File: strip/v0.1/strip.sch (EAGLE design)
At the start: 96 parts, among them IC1 LP2992, IC2 ADP3110A-SO8, IC3 STM32-M-48, IC4 OPA335, IC5 ADP3110A-SO8, IC6 ADP3110A-SO8, Q1 IRF7828, Q2 IRF7828, Q3 IRF7828, Q4 IRF7828, Q5 IRF7828, Q6 IRF7828

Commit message: All airwires routed. Now polishing can begin.
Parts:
- removed R32: 1k, pel_dipol_comp:RESISTOR-0402
- removed TH1: 2kOhm, pel_dipol_comp:RESISTOR-0402
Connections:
- removed net TEMP: IC3.PA5-SPI1SCK/ADC5, R32.2, TH1.1
- net +3V3: no longer R32.1
- net GND: no longer TH1.2
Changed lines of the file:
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@@
 <part name="GND16" library="supply1" deviceset="GND" device=""/>
 <part name="GND20" library="supply1" deviceset="GND" device=""/>
-<part name="TH1" library="pel_dipol_comp" deviceset="RESISTOR" device="-0402" value="2kOhm"/>
-<part name="R32" library="pel_dipol_comp" deviceset="RESISTOR" device="-0402" value="1k"/>
-<part name="P+6" library="supply1" deviceset="+3V3" device=""/>
-<part name="GND21" library="supply1" deviceset="GND" device=""/>
 <part name="L1" library="res_cap" deviceset="INDUCTOR" device="-0603" value=""/>
 <part name="C19" library="pel_dipol_comp" deviceset="CAPACITOR" device="-0402" value="100nF"/>
@@
 <instance part="GND16" gate="1" x="317.5" y="40.64"/>
 <instance part="GND20" gate="1" x="312.42" y="60.96"/>
-<instance part="TH1" gate="G$1" x="236.22" y="116.84" rot="R270"/>
-<instance part="R32" gate="G$1" x="236.22" y="127" rot="R270"/>
-<instance part="P+6" gate="G$1" x="236.22" y="137.16"/>
-<instance part="GND21" gate="1" x="236.22" y="109.22"/>
 <instance part="L1" gate="G$1" x="325.12" y="101.6" rot="R180"/>
 <instance part="C19" gate="G$1" x="335.28" y="93.98" rot="R270"/>
@@
 </segment>
 <segment>
-<pinref part="TH1" gate="G$1" pin="2"/>
-<pinref part="GND21" gate="1" pin="GND"/>
-</segment>
-<segment>
 <wire x1="60.96" y1="88.9" x2="58.42" y2="88.9" width="0.1524" layer="91"/>
 <wire x1="58.42" y1="88.9" x2="58.42" y2="83.82" width="0.1524" layer="91"/>
@@
 </segment>
 <segment>
-<wire x1="236.22" y1="134.62" x2="236.22" y2="132.08" width="0.1524" layer="91"/>
-<pinref part="R32" gate="G$1" pin="1"/>
-<pinref part="P+6" gate="G$1" pin="+3V3"/>
-</segment>
-<segment>
 <wire x1="60.96" y1="96.52" x2="58.42" y2="96.52" width="0.1524" layer="91"/>
 <wire x1="58.42" y1="96.52" x2="58.42" y2="99.06" width="0.1524" layer="91"/>
@@
 </segment>
 </net>
-<net name="TEMP" class="0">
-<segment>
-<wire x1="63.5" y1="167.64" x2="45.72" y2="167.64" width="0.1524" layer="91"/>
-<label x="63.5" y="167.64" size="1.778" layer="95" rot="MR0"/>
-<pinref part="IC3" gate="G$1" pin="PA5-SPI1SCK/ADC5"/>
-</segment>
-<segment>
-<wire x1="236.22" y1="121.92" x2="224.79" y2="121.92" width="0.1524" layer="91"/>
-<wire x1="224.79" y1="121.92" x2="218.44" y2="121.92" width="0.1524" layer="91"/>
-<junction x="236.22" y="121.92"/>
-<label x="218.44" y="121.92" size="1.778" layer="95" rot="R180" xref="yes"/>
-<pinref part="TH1" gate="G$1" pin="1"/>
-<pinref part="R32" gate="G$1" pin="2"/>
-</segment>
-</net>

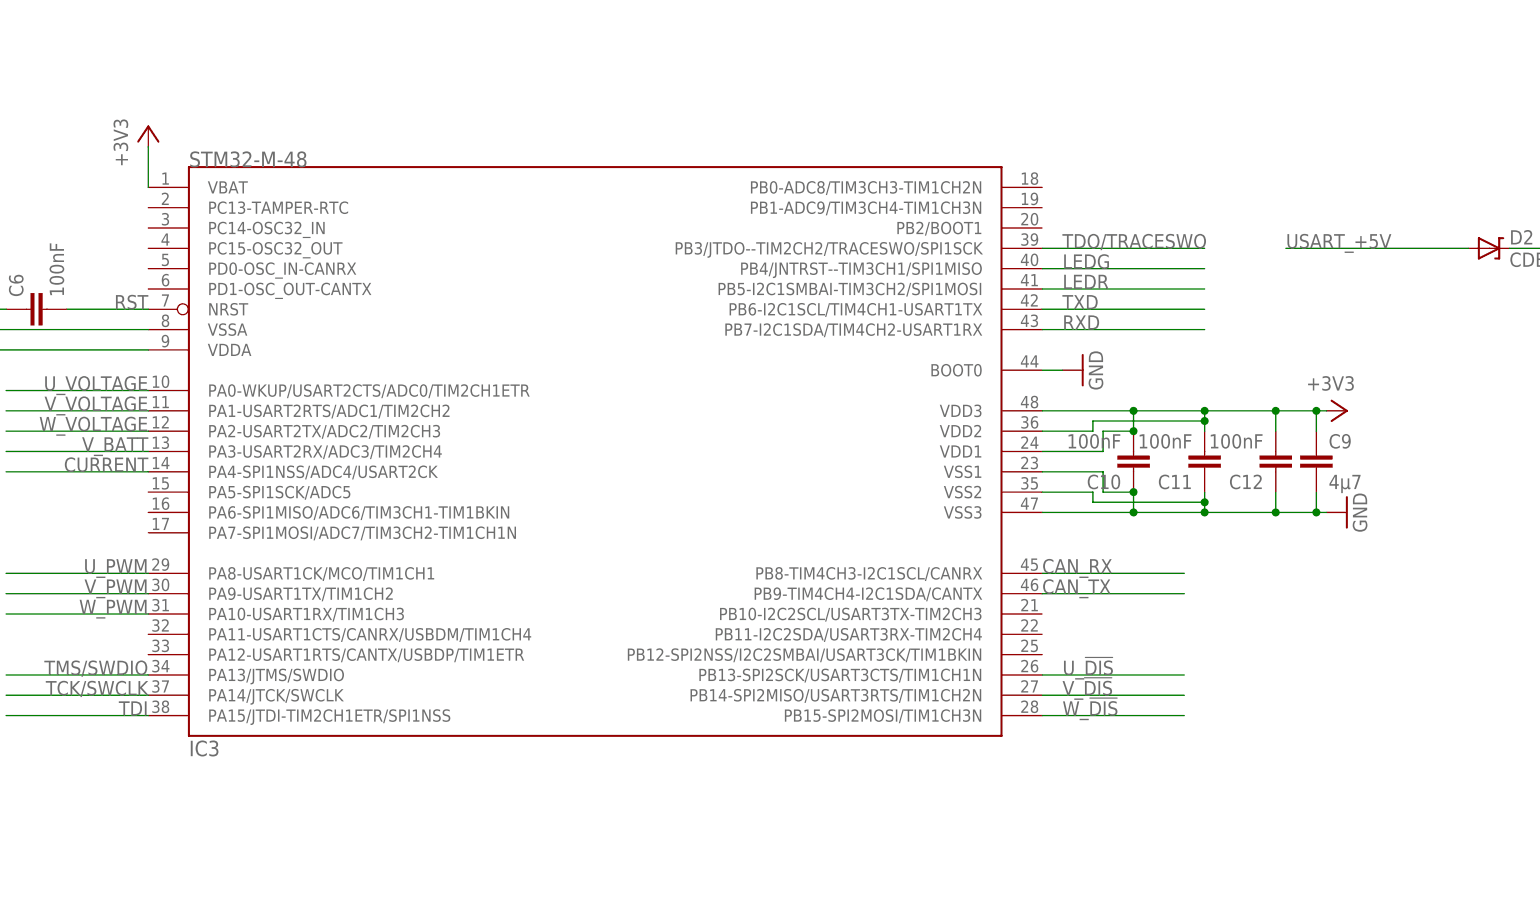
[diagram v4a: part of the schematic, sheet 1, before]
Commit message: Added power rail tantalum capacitor.
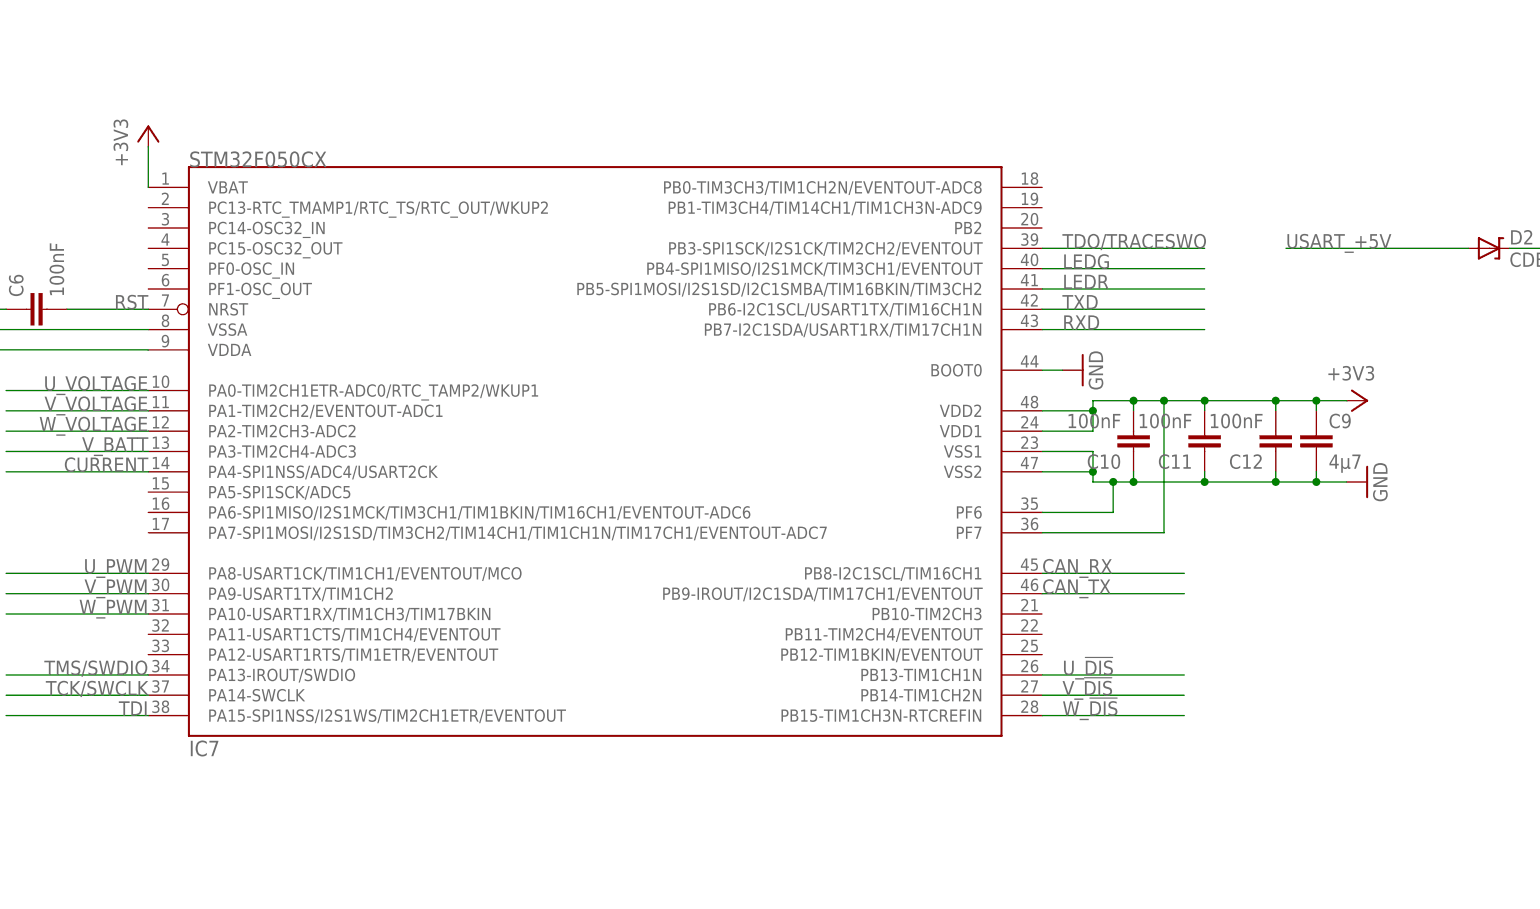
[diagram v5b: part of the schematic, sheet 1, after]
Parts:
- removed IC3: STM32-M-48, pel_stm32:STM32-M-48
- added C5: (no value), pel_dipol_comp:CAPACITOR-POLD
- added IC7: STM32F050CX, pel_stm32:STM32F050CX
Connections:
- net +3V3: now also IC7.PF7, IC7.VBAT, IC7.VDD1, IC7.VDD2; no longer IC3.VBAT, IC3.VDD1, IC3.VDD2, IC3.VDD3
- net BUSS+: now also C5.+
- net CAN_RX: now also IC7.PB8-I2C1SCL/TIM16CH1; no longer IC3.PB8-TIM4CH3-I2C1SCL/CANRX
- net CAN_TX: now also IC7.PB9-IROUT/I2C1SDA/TIM17CH1/EVENTOUT; no longer IC3.PB9-TIM4CH4-I2C1SDA/CANTX
- net CURRENT: now also IC7.PA4-SPI1NSS/ADC4/USART2CK; no longer IC3.PA4-SPI1NSS/ADC4/USART2CK
- net GND: now also C5.-, IC7.BOOT0, IC7.PF6, IC7.VSS1, IC7.VSS2, IC7.VSSA; no longer IC3.BOOT0, IC3.VSS1, IC3.VSS2, IC3.VSS3, IC3.VSSA
- net LEDG: now also IC7.PB4-SPI1MISO/I2S1MCK/TIM3CH1/EVENTOUT; no longer IC3.PB4/JNTRST--TIM3CH1/SPI1MISO
- net LEDR: now also IC7.PB5-SPI1MOSI/I2S1SD/I2C1SMBA/TIM16BKIN/TIM3CH2; no longer IC3.PB5-I2C1SMBAI-TIM3CH2/SPI1MOSI
- net RST: now also IC7.NRST; no longer IC3.NRST
- net RXD: now also IC7.PB7-I2C1SDA/USART1RX/TIM17CH1N; no longer IC3.PB7-I2C1SDA/TIM4CH2-USART1RX
- net TCK/SWCLK: now also IC7.PA14-SWCLK; no longer IC3.PA14/JTCK/SWCLK
- net TDI: now also IC7.PA15-SPI1NSS/I2S1WS/TIM2CH1ETR/EVENTOUT; no longer IC3.PA15/JTDI-TIM2CH1ETR/SPI1NSS
- net TDO/TRACESWO: now also IC7.PB3-SPI1SCK/I2S1CK/TIM2CH2/EVENTOUT; no longer IC3.PB3/JTDO--TIM2CH2/TRACESWO/SPI1SCK
- net TMS/SWDIO: now also IC7.PA13-IROUT/SWDIO; no longer IC3.PA13/JTMS/SWDIO
- net TXD: now also IC7.PB6-I2C1SCL/USART1TX/TIM16CH1N; no longer IC3.PB6-I2C1SCL/TIM4CH1-USART1TX
- net U_!DIS: now also IC7.PB13-TIM1CH1N; no longer IC3.PB13-SPI2SCK/USART3CTS/TIM1CH1N
- net U_PWM: now also IC7.PA8-USART1CK/TIM1CH1/EVENTOUT/MCO; no longer IC3.PA8-USART1CK/MCO/TIM1CH1
- net U_VOLTAGE: now also IC7.PA0-TIM2CH1ETR-ADC0/RTC_TAMP2/WKUP1; no longer IC3.PA0-WKUP/USART2CTS/ADC0/TIM2CH1ETR
- net VDDA: now also IC7.VDDA; no longer IC3.VDDA
- net V_!DIS: now also IC7.PB14-TIM1CH2N; no longer IC3.PB14-SPI2MISO/USART3RTS/TIM1CH2N
- net V_BATT: now also IC7.PA3-TIM2CH4-ADC3; no longer IC3.PA3-USART2RX/ADC3/TIM2CH4
- net V_PWM: now also IC7.PA9-USART1TX/TIM1CH2; no longer IC3.PA9-USART1TX/TIM1CH2
- net V_VOLTAGE: now also IC7.PA1-TIM2CH2/EVENTOUT-ADC1; no longer IC3.PA1-USART2RTS/ADC1/TIM2CH2
- net W_!DIS: now also IC7.PB15-TIM1CH3N-RTCREFIN; no longer IC3.PB15-SPI2MOSI/TIM1CH3N
- net W_PWM: now also IC7.PA10-USART1RX/TIM1CH3/TIM17BKIN; no longer IC3.PA10-USART1RX/TIM1CH3
- net W_VOLTAGE: now also IC7.PA2-TIM2CH3-ADC2; no longer IC3.PA2-USART2TX/ADC2/TIM2CH3
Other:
- moved on the sheet: C10, C11, C12, C9

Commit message: Added silkscreen obldc logo. Put the logo and text on the pcb.
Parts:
- U$1: device open-bldc:LOGO-NORM -> open-bldc:LOGO-SILK-SMALL
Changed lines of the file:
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@@
 <part name="R4" library="pel_dipol_comp" deviceset="RESISTOR" device="-0402" value="1k"/>
 <part name="FRAME1" library="frames" deviceset="A3L-LOC" device=""/>
-<part name="U$1" library="open-bldc" deviceset="LOGO" device="-NORM" value="LOGO"/>
+<part name="U$1" library="open-bldc" deviceset="LOGO" device="-SILK-SMALL" value="LOGO"/>
 <part name="GND13" library="supply1" deviceset="GND" device=""/>
 <part name="+3V2" library="supply1" deviceset="+3V3" device=""/>

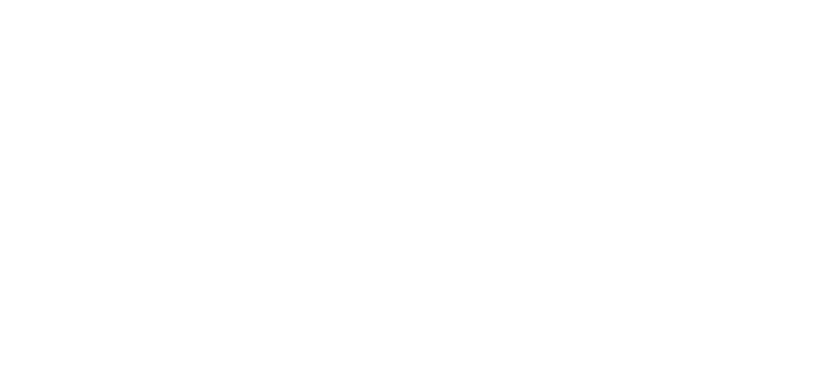
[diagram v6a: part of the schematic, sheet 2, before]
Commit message: Corrected size of the 4.7uF capacitor for the STM32.
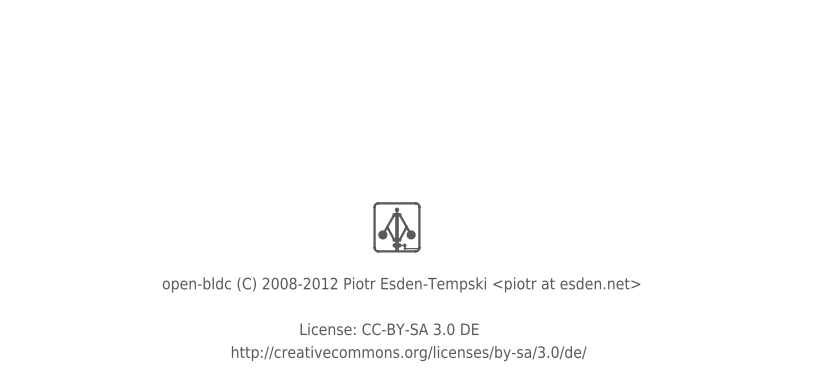
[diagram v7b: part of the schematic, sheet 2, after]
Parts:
- added U$2: LOGO, open-bldc:LOGO-SILK-SMALL
- C9: device pel_dipol_comp:CAPACITOR-0402 -> pel_dipol_comp:CAPACITOR-0805
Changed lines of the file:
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@@
 <setting verticaltext="up"/>
 </settings>
-<grid distance="0.05" unitdist="inch" unit="inch" style="lines" multiple="1" display="no" altdistance="0.01" altunitdist="inch" altunit="inch"/>
+<grid distance="0.1" unitdist="inch" unit="inch" style="lines" multiple="1" display="no" altdistance="0.01" altunitdist="inch" altunit="inch"/>
 <layers>
 <layer number="1" name="Top" color="4" fill="1" visible="no" active="no"/>
@@
 <part name="C11" library="pel_dipol_comp" deviceset="CAPACITOR" device="-0402" value="100nF"/>
 <part name="C12" library="pel_dipol_comp" deviceset="CAPACITOR" device="-0402" value="100nF"/>
-<part name="C9" library="pel_dipol_comp" deviceset="CAPACITOR" device="-0402" value="4µ7"/>
+<part name="C9" library="pel_dipol_comp" deviceset="CAPACITOR" device="-0805" value="4µ7"/>
 <part name="GND1" library="supply1" deviceset="GND" device=""/>
 <part name="P+13" library="supply1" deviceset="+3V3" device=""/>
@@
 <part name="IC7" library="pel_stm32" deviceset="STM32F050CX" device=""/>
 <part name="C5" library="pel_dipol_comp" deviceset="CAPACITOR-POL" device="D"/>
+<part name="U$2" library="open-bldc" deviceset="LOGO" device="-SILK-SMALL" value="LOGO"/>
 </parts>
 <sheets>
@@
 <text x="185.42" y="223.52" size="1.778" layer="95">BUSS+ PAD</text>
 <text x="185.42" y="198.12" size="1.778" layer="95">BUSS- PAD</text>
+<text x="304.292" y="7.62" size="1.27" layer="97">License: CC-BY-SA 3.0 DE</text>
+<text x="296.672" y="5.08" size="1.27" layer="97">http://creativecommons.org/licenses/by-sa/3.0/de/</text>
+<text x="289.052" y="12.7" size="1.27" layer="97">open-bldc (C) 2008-2012 Piotr Esden-Tempski &lt;piotr at esden.net&gt;</text>
 </plain>
 <instances>
@@
 <instance part="R10" gate="G$1" x="132.08" y="66.04"/>
 <instance part="C5" gate="G$1" x="189.23" y="213.36"/>
+<instance part="U$2" gate="G$1" x="315.214" y="19.304"/>
 </instances>
 <busses>
